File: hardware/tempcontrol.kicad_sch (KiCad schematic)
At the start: 17 parts, among them J10 FAN2, J9 FAN1, U12 EMC2305-x-AP

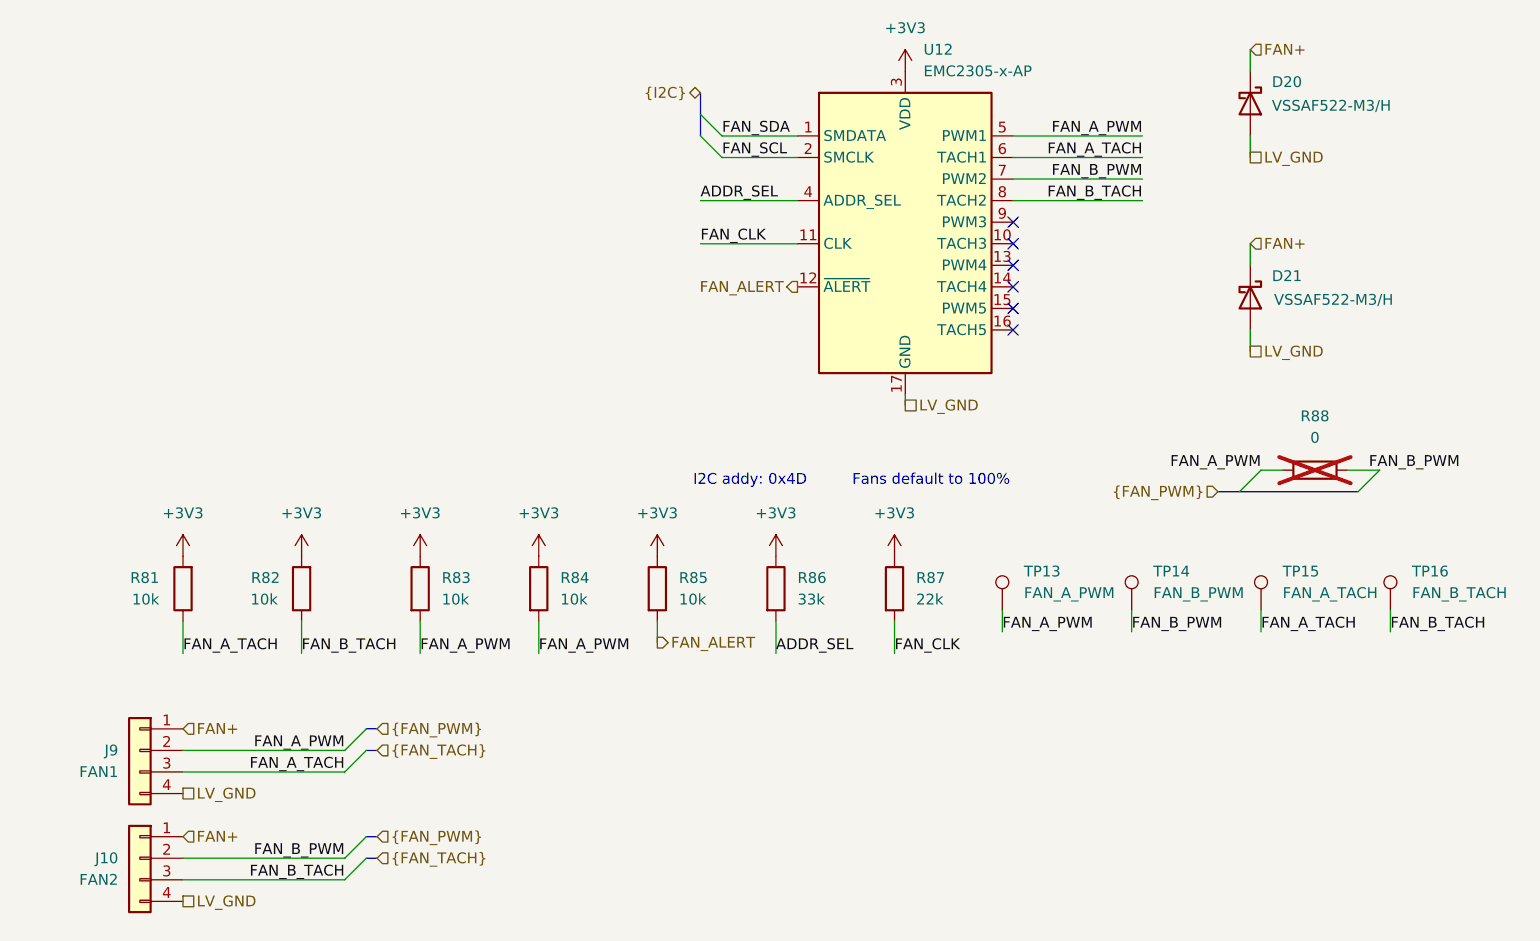
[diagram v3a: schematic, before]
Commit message: fixed up labels
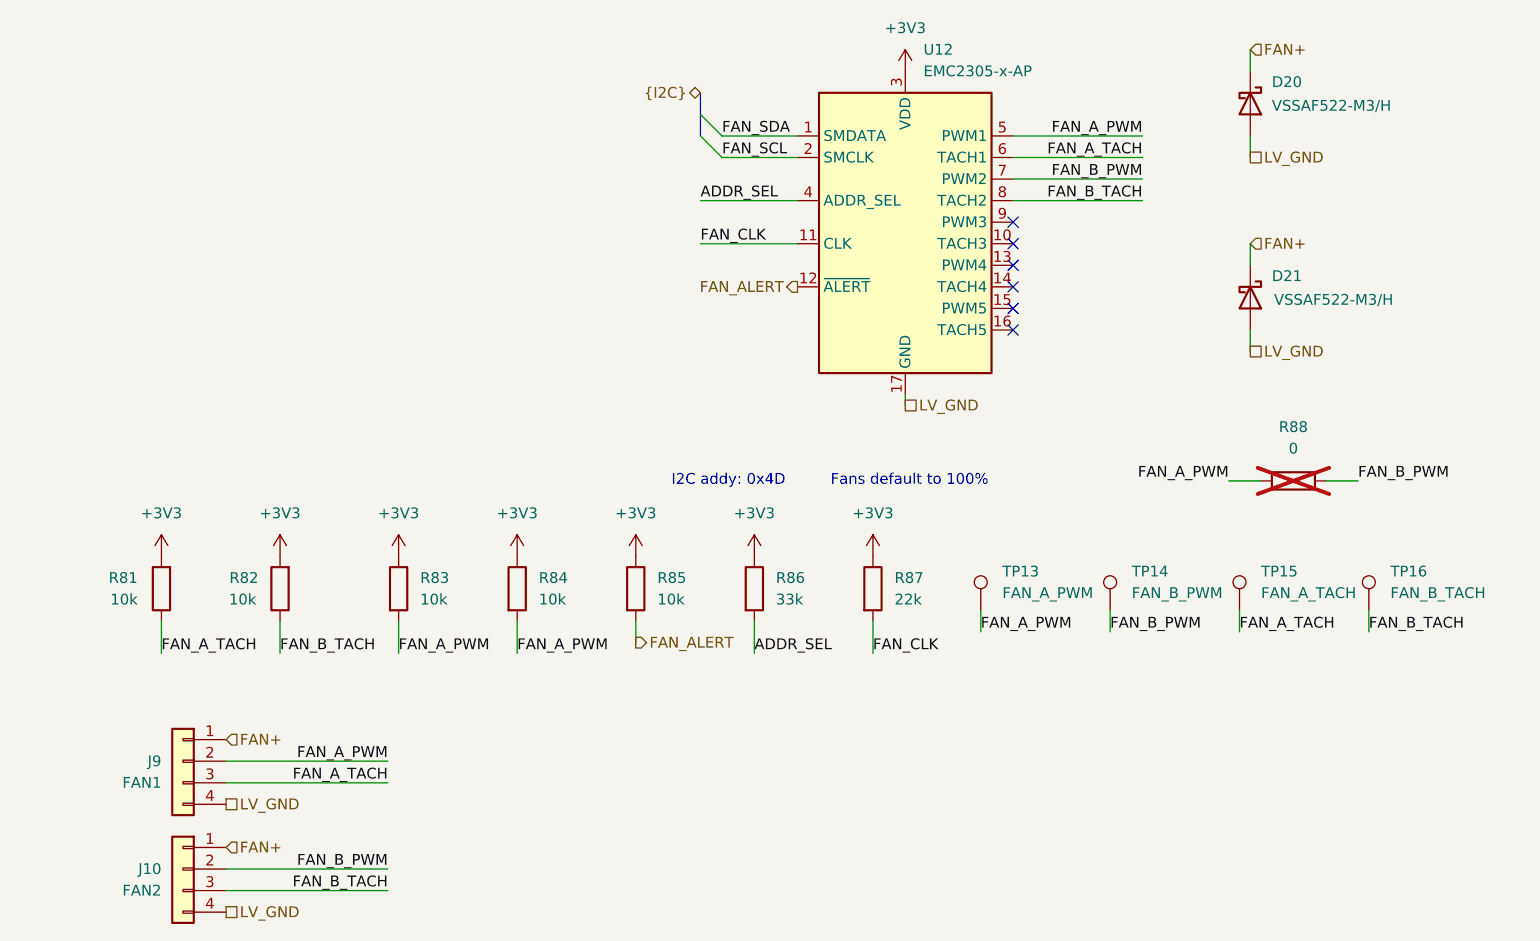
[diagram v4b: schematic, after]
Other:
- moved on the sheet: J10, J9, R81, R82, R83, R84, R85, R86, R87, R88, TP13, TP14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

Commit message: switch branch
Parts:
- renumbered R81 to R86, R82 to R87, R83 to R88, R84 to R89, R85 to R90, R86 to R91, R87 to R92, R88 to R93, TP13 to TP17, TP14 to TP18, TP15 to TP19, TP16 to TP20
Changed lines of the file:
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@@
 		(dnp no)
 		(fields_autoplaced yes)
-		(property "Reference" "R85"
+		(property "Reference" "R90"
 			(at 95.25 88.8999 0)
 			(show_name no)
@@
 			(project "PS-LVCarrier"
 				(path "/9bab2d9d-20f3-40ef-8545-e1299efec47e/f9fba8b7-0cf3-4419-9ae4-4e9c55277e07"
-					(reference "R85")
+					(reference "R90")
 					(unit 1)
 				)
@@
 		(dnp no)
 		(fields_autoplaced yes)
-		(property "Reference" "R84"
+		(property "Reference" "R89"
 			(at 81.28 88.8999 0)
 			(show_name no)
@@
 			(project "PS-LVCarrier"
 				(path "/9bab2d9d-20f3-40ef-8545-e1299efec47e/f9fba8b7-0cf3-4419-9ae4-4e9c55277e07"
-					(reference "R84")
+					(reference "R89")
 					(unit 1)
 				)
@@
 		(dnp no)
 		(fields_autoplaced yes)
-		(property "Reference" "TP16"
+		(property "Reference" "TP20"
 			(at 181.61 88.1379 0)
 			(show_name no)
@@
 			(project "PS-LVCarrier"
 				(path "/9bab2d9d-20f3-40ef-8545-e1299efec47e/f9fba8b7-0cf3-4419-9ae4-4e9c55277e07"
-					(reference "TP16")
+					(reference "TP20")
 					(unit 1)
 				)
@@
 		(dnp no)
 		(fields_autoplaced yes)
-		(property "Reference" "#PWR0104"
+		(property "Reference" "#PWR086"
 			(at 124.46 33.02 0)
 			(hide yes)
@@
 			(project "PS-LVCarrier"
 				(path "/9bab2d9d-20f3-40ef-8545-e1299efec47e/f9fba8b7-0cf3-4419-9ae4-4e9c55277e07"
-					(reference "#PWR0104")
+					(reference "#PWR086")
 					(unit 1)
 				)
@@
 		(dnp no)
 		(fields_autoplaced yes)
-		(property "Reference" "R83"
+		(property "Reference" "R88"
 			(at 67.31 88.8999 0)
 			(show_name no)
@@
 			(project "PS-LVCarrier"
 				(path "/9bab2d9d-20f3-40ef-8545-e1299efec47e/f9fba8b7-0cf3-4419-9ae4-4e9c55277e07"
-					(reference "R83")
+					(reference "R88")
 					(unit 1)
 				)
@@
 		(dnp no)
 		(fields_autoplaced yes)
-		(property "Reference" "#PWR097"
+		(property "Reference" "#PWR079"
 			(at 36.83 90.17 0)
 			(hide yes)
@@
 			(project "PS-LVCarrier"
 				(path "/9bab2d9d-20f3-40ef-8545-e1299efec47e/f9fba8b7-0cf3-4419-9ae4-4e9c55277e07"
-					(reference "#PWR097")
+					(reference "#PWR079")
 					(unit 1)
 				)
@@
 		(dnp no)
 		(fields_autoplaced yes)
-		(property "Reference" "TP15"
+		(property "Reference" "TP19"
 			(at 166.37 88.1379 0)
 			(show_name no)
@@
 			(project "PS-LVCarrier"
 				(path "/9bab2d9d-20f3-40ef-8545-e1299efec47e/f9fba8b7-0cf3-4419-9ae4-4e9c55277e07"
-					(reference "TP15")
+					(reference "TP19")
 					(unit 1)
 				)
@@
 		(in_pos_files yes)
 		(dnp no)
-		(property "Reference" "R82"
+		(property "Reference" "R87"
 			(at 48.26 88.9 0)
 			(show_name no)
@@
 			(project "PS-LVCarrier"
 				(path "/9bab2d9d-20f3-40ef-8545-e1299efec47e/f9fba8b7-0cf3-4419-9ae4-4e9c55277e07"
-					(reference "R82")
+					(reference "R87")
 					(unit 1)
 				)
@@
 		(dnp no)
 		(fields_autoplaced yes)
-		(property "Reference" "#PWR0100"
+		(property "Reference" "#PWR082"
 			(at 78.74 90.17 0)
 			(hide yes)
@@
 			(project "PS-LVCarrier"
 				(path "/9bab2d9d-20f3-40ef-8545-e1299efec47e/f9fba8b7-0cf3-4419-9ae4-4e9c55277e07"
-					(reference "#PWR0100")
+					(reference "#PWR082")
 					(unit 1)
 				)
@@
 		(dnp no)
 		(fields_autoplaced yes)
-		(property "Reference" "#PWR0101"
+		(property "Reference" "#PWR083"
 			(at 92.71 90.17 0)
 			(hide yes)
@@
 			(project "PS-LVCarrier"
 				(path "/9bab2d9d-20f3-40ef-8545-e1299efec47e/f9fba8b7-0cf3-4419-9ae4-4e9c55277e07"
-					(reference "#PWR0101")
+					(reference "#PWR083")
 					(unit 1)
 				)
@@
 		(dnp no)
 		(fields_autoplaced yes)
-		(property "Reference" "#PWR099"
+		(property "Reference" "#PWR081"
 			(at 64.77 90.17 0)
 			(hide yes)
@@
 			(project "PS-LVCarrier"
 				(path "/9bab2d9d-20f3-40ef-8545-e1299efec47e/f9fba8b7-0cf3-4419-9ae4-4e9c55277e07"
-					(reference "#PWR099")
+					(reference "#PWR081")
 					(unit 1)
 				)
@@
 		(dnp no)
 		(fields_autoplaced yes)
-		(property "Reference" "R86"
+		(property "Reference" "R91"
 			(at 109.22 88.8999 0)
 			(show_name no)
@@
 			(project "PS-LVCarrier"
 				(path "/9bab2d9d-20f3-40ef-8545-e1299efec47e/f9fba8b7-0cf3-4419-9ae4-4e9c55277e07"
-					(reference "R86")
+					(reference "R91")
 					(unit 1)
 				)
@@
 		(dnp no)
 		(fields_autoplaced yes)
-		(property "Reference" "TP14"
+		(property "Reference" "TP18"
 			(at 151.13 88.1379 0)
 			(show_name no)
@@
 			(project "PS-LVCarrier"
 				(path "/9bab2d9d-20f3-40ef-8545-e1299efec47e/f9fba8b7-0cf3-4419-9ae4-4e9c55277e07"
-					(reference "TP14")
+					(reference "TP18")
 					(unit 1)
 				)
@@
 		(dnp no)
 		(fields_autoplaced yes)
-		(property "Reference" "TP13"
+		(property "Reference" "TP17"
 			(at 135.89 88.1379 0)
 			(show_name no)
@@
 			(project "PS-LVCarrier"
 				(path "/9bab2d9d-20f3-40ef-8545-e1299efec47e/f9fba8b7-0cf3-4419-9ae4-4e9c55277e07"
-					(reference "TP13")
+					(reference "TP17")
 					(unit 1)
 				)
@@
 		(dnp no)
 		(fields_autoplaced yes)
-		(property "Reference" "#PWR0103"
+		(property "Reference" "#PWR085"
 			(at 120.65 90.17 0)
 			(hide yes)
@@
 			(project "PS-LVCarrier"
 				(path "/9bab2d9d-20f3-40ef-8545-e1299efec47e/f9fba8b7-0cf3-4419-9ae4-4e9c55277e07"
-					(reference "#PWR0103")
+					(reference "#PWR085")
 					(unit 1)
 				)
@@
 		(dnp no)
 		(fields_autoplaced yes)
-		(property "Reference" "R87"
+		(property "Reference" "R92"
 			(at 123.19 88.8999 0)
 			(show_name no)
@@
 			(project "PS-LVCarrier"
 				(path "/9bab2d9d-20f3-40ef-8545-e1299efec47e/f9fba8b7-0cf3-4419-9ae4-4e9c55277e07"
-					(reference "R87")
+					(reference "R92")
 					(unit 1)
 				)
@@
 		(dnp yes)
 		(fields_autoplaced yes)
-		(property "Reference" "R88"
+		(property "Reference" "R93"
 			(at 170.18 71.12 90)
 			(show_name no)
@@
 			(project "PS-LVCarrier"
 				(path "/9bab2d9d-20f3-40ef-8545-e1299efec47e/f9fba8b7-0cf3-4419-9ae4-4e9c55277e07"
-					(reference "R88")
+					(reference "R93")
 					(unit 1)
 				)
@@
 		(in_pos_files yes)
 		(dnp no)
-		(property "Reference" "R81"
+		(property "Reference" "R86"
 			(at 34.036 88.9 0)
 			(show_name no)
@@
 			(project "PS-LVCarrier"
 				(path "/9bab2d9d-20f3-40ef-8545-e1299efec47e/f9fba8b7-0cf3-4419-9ae4-4e9c55277e07"
-					(reference "R81")
+					(reference "R86")
 					(unit 1)
 				)
@@
 		(dnp no)
 		(fields_autoplaced yes)
-		(property "Reference" "#PWR098"
+		(property "Reference" "#PWR080"
 			(at 50.8 90.17 0)
 			(hide yes)
@@
 			(project "PS-LVCarrier"
 				(path "/9bab2d9d-20f3-40ef-8545-e1299efec47e/f9fba8b7-0cf3-4419-9ae4-4e9c55277e07"
-					(reference "#PWR098")
+					(reference "#PWR080")
 					(unit 1)
 				)
@@
 		(dnp no)
 		(fields_autoplaced yes)
-		(property "Reference" "#PWR0102"
+		(property "Reference" "#PWR084"
 			(at 106.68 90.17 0)
 			(hide yes)
@@
 			(project "PS-LVCarrier"
 				(path "/9bab2d9d-20f3-40ef-8545-e1299efec47e/f9fba8b7-0cf3-4419-9ae4-4e9c55277e07"
-					(reference "#PWR0102")
-					(unit 1)
-				)
+					(reference "#PWR084")
+					(unit 1)
+				)

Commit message: most reviews addressed oops
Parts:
- removed D21: VSSAF522-M3/H, UTSVT_Passive:SODFL5026X125N, symbol Diode:C3D25170H
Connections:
- net +3V3: no longer U12.3 (VDD)
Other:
- moved on the sheet: D20, J10, J9, U12

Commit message: progress!
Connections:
- net +3V3: now also U12.3 (VDD)
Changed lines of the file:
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@@
 	(symbol
 		(lib_id "power:+3V3")
-		(at 124.46 29.21 0)
+		(at 130.81 29.21 0)
 		(unit 1)
 		(body_style 1)
@@
 		(fields_autoplaced yes)
 		(property "Reference" "#PWR086"
-			(at 124.46 33.02 0)
+			(at 130.81 33.02 0)
 			(hide yes)
 			(show_name no)
@@
 		)
 		(property "Value" "+3V3"
-			(at 124.46 24.13 0)
+			(at 130.81 24.13 0)
 			(show_name no)
 			(do_not_autoplace no)
@@
 		)
 		(property "Footprint" ""
-			(at 124.46 29.21 0)
+			(at 130.81 29.21 0)
 			(hide yes)
 			(show_name no)
@@
 		)
 		(property "Datasheet" ""
-			(at 124.46 29.21 0)
+			(at 130.81 29.21 0)
 			(hide yes)
 			(show_name no)
@@
 		)
 		(property "Description" "Power symbol creates a global label with name \"+3V3\""
-			(at 124.46 29.21 0)
+			(at 130.81 29.21 0)
 			(hide yes)
 			(show_name no)

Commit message: review ts
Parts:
- renumbered D20 to D7, J10 to J7, J9 to J8, R86 to R19, R87 to R20, R88 to R21, R89 to R22, R90 to R23, R91 to R24, R92 to R25, R93 to R26, TP17 to TP5, TP18 to TP6, TP19 to TP7, TP20 to TP8, U12 to U2
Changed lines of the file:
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@@
 		(dnp no)
 		(fields_autoplaced yes)
-		(property "Reference" "U12"
+		(property "Reference" "U2"
 			(at 134.112 26.416 0)
 			(show_name no)
@@
 			(project "PS-LVCarrier"
 				(path "/9bab2d9d-20f3-40ef-8545-e1299efec47e/f9fba8b7-0cf3-4419-9ae4-4e9c55277e07"
-					(reference "U12")
+					(reference "U2")
 					(unit 1)
 				)
@@
 		(dnp no)
 		(fields_autoplaced yes)
-		(property "Reference" "R90"
+		(property "Reference" "R23"
 			(at 95.25 88.8999 0)
 			(show_name no)
@@
 			(project "PS-LVCarrier"
 				(path "/9bab2d9d-20f3-40ef-8545-e1299efec47e/f9fba8b7-0cf3-4419-9ae4-4e9c55277e07"
-					(reference "R90")
+					(reference "R23")
 					(unit 1)
 				)
@@
 		(dnp no)
 		(fields_autoplaced yes)
-		(property "Reference" "R89"
+		(property "Reference" "R22"
 			(at 81.28 88.8999 0)
 			(show_name no)
@@
 			(project "PS-LVCarrier"
 				(path "/9bab2d9d-20f3-40ef-8545-e1299efec47e/f9fba8b7-0cf3-4419-9ae4-4e9c55277e07"
-					(reference "R89")
+					(reference "R22")
 					(unit 1)
 				)
@@
 		(dnp no)
 		(fields_autoplaced yes)
-		(property "Reference" "TP20"
+		(property "Reference" "TP8"
 			(at 181.61 88.1379 0)
 			(show_name no)
@@
 			(project "PS-LVCarrier"
 				(path "/9bab2d9d-20f3-40ef-8545-e1299efec47e/f9fba8b7-0cf3-4419-9ae4-4e9c55277e07"
-					(reference "TP20")
+					(reference "TP8")
 					(unit 1)
 				)
@@
 		(dnp no)
 		(fields_autoplaced yes)
-		(property "Reference" "#PWR086"
+		(property "Reference" "#PWR031"
 			(at 130.81 33.02 0)
 			(hide yes)
@@
 			(project "PS-LVCarrier"
 				(path "/9bab2d9d-20f3-40ef-8545-e1299efec47e/f9fba8b7-0cf3-4419-9ae4-4e9c55277e07"
-					(reference "#PWR086")
+					(reference "#PWR031")
 					(unit 1)
 				)
@@
 		(dnp no)
 		(fields_autoplaced yes)
-		(property "Reference" "R88"
+		(property "Reference" "R21"
 			(at 67.31 88.8999 0)
 			(show_name no)
@@
 			(project "PS-LVCarrier"
 				(path "/9bab2d9d-20f3-40ef-8545-e1299efec47e/f9fba8b7-0cf3-4419-9ae4-4e9c55277e07"
-					(reference "R88")
+					(reference "R21")
 					(unit 1)
 				)
@@
 		(dnp no)
 		(fields_autoplaced yes)
-		(property "Reference" "#PWR079"
+		(property "Reference" "#PWR024"
 			(at 36.83 90.17 0)
 			(hide yes)
@@
 			(project "PS-LVCarrier"
 				(path "/9bab2d9d-20f3-40ef-8545-e1299efec47e/f9fba8b7-0cf3-4419-9ae4-4e9c55277e07"
-					(reference "#PWR079")
+					(reference "#PWR024")
 					(unit 1)
 				)
@@
 		(dnp no)
 		(fields_autoplaced yes)
-		(property "Reference" "TP19"
+		(property "Reference" "TP7"
 			(at 166.37 88.1379 0)
 			(show_name no)
@@
 			(project "PS-LVCarrier"
 				(path "/9bab2d9d-20f3-40ef-8545-e1299efec47e/f9fba8b7-0cf3-4419-9ae4-4e9c55277e07"
-					(reference "TP19")
+					(reference "TP7")
 					(unit 1)
 				)
@@
 		(in_pos_files yes)
 		(dnp no)
-		(property "Reference" "R87"
+		(property "Reference" "R20"
 			(at 48.26 88.9 0)
 			(show_name no)
@@
 			(project "PS-LVCarrier"
 				(path "/9bab2d9d-20f3-40ef-8545-e1299efec47e/f9fba8b7-0cf3-4419-9ae4-4e9c55277e07"
-					(reference "R87")
+					(reference "R20")
 					(unit 1)
 				)
@@
 		(dnp no)
 		(fields_autoplaced yes)
-		(property "Reference" "#PWR082"
+		(property "Reference" "#PWR027"
 			(at 78.74 90.17 0)
 			(hide yes)
@@
 			(project "PS-LVCarrier"
 				(path "/9bab2d9d-20f3-40ef-8545-e1299efec47e/f9fba8b7-0cf3-4419-9ae4-4e9c55277e07"
-					(reference "#PWR082")
+					(reference "#PWR027")
 					(unit 1)
 				)
@@
 		(dnp no)
 		(fields_autoplaced yes)
-		(property "Reference" "#PWR083"
+		(property "Reference" "#PWR028"
 			(at 92.71 90.17 0)
 			(hide yes)
@@
 			(project "PS-LVCarrier"
 				(path "/9bab2d9d-20f3-40ef-8545-e1299efec47e/f9fba8b7-0cf3-4419-9ae4-4e9c55277e07"
-					(reference "#PWR083")
+					(reference "#PWR028")
 					(unit 1)
 				)
@@
 		(dnp no)
 		(fields_autoplaced yes)
-		(property "Reference" "#PWR081"
+		(property "Reference" "#PWR026"
 			(at 64.77 90.17 0)
 			(hide yes)
@@
 			(project "PS-LVCarrier"
 				(path "/9bab2d9d-20f3-40ef-8545-e1299efec47e/f9fba8b7-0cf3-4419-9ae4-4e9c55277e07"
-					(reference "#PWR081")
+					(reference "#PWR026")
 					(unit 1)
 				)
@@
 		(dnp no)
 		(fields_autoplaced yes)
-		(property "Reference" "R91"
+		(property "Reference" "R24"
 			(at 109.22 88.8999 0)
 			(show_name no)
@@
 			(project "PS-LVCarrier"
 				(path "/9bab2d9d-20f3-40ef-8545-e1299efec47e/f9fba8b7-0cf3-4419-9ae4-4e9c55277e07"
-					(reference "R91")
+					(reference "R24")
 					(unit 1)
 				)
@@
 		(in_pos_files yes)
 		(dnp no)
-		(property "Reference" "J9"
+		(property "Reference" "J8"
 			(at 59.69 114.2999 0)
 			(show_name no)
@@
 			(project "PS-LVCarrier"
 				(path "/9bab2d9d-20f3-40ef-8545-e1299efec47e/f9fba8b7-0cf3-4419-9ae4-4e9c55277e07"
-					(reference "J9")
+					(reference "J8")
 					(unit 1)
 				)
@@
 		(in_pos_files yes)
 		(dnp no)
-		(property "Reference" "J10"
+		(property "Reference" "J7"
 			(at 25.4 114.2999 0)
 			(show_name no)
@@
 			(project "PS-LVCarrier"
 				(path "/9bab2d9d-20f3-40ef-8545-e1299efec47e/f9fba8b7-0cf3-4419-9ae4-4e9c55277e07"
-					(reference "J10")
+					(reference "J7")
 					(unit 1)
 				)
@@
 		(dnp no)
 		(fields_autoplaced yes)
-		(property "Reference" "TP18"
+		(property "Reference" "TP6"
 			(at 151.13 88.1379 0)
 			(show_name no)
@@
 			(project "PS-LVCarrier"
 				(path "/9bab2d9d-20f3-40ef-8545-e1299efec47e/f9fba8b7-0cf3-4419-9ae4-4e9c55277e07"
-					(reference "TP18")
+					(reference "TP6")
 					(unit 1)
 				)
@@
 		(dnp no)
 		(fields_autoplaced yes)
-		(property "Reference" "TP17"
+		(property "Reference" "TP5"
 			(at 135.89 88.1379 0)
 			(show_name no)
@@
 			(project "PS-LVCarrier"
 				(path "/9bab2d9d-20f3-40ef-8545-e1299efec47e/f9fba8b7-0cf3-4419-9ae4-4e9c55277e07"
-					(reference "TP17")
+					(reference "TP5")
 					(unit 1)
 				)
@@
 		(dnp no)
 		(fields_autoplaced yes)
-		(property "Reference" "#PWR085"
+		(property "Reference" "#PWR030"
 			(at 120.65 90.17 0)
 			(hide yes)
@@
 			(project "PS-LVCarrier"
 				(path "/9bab2d9d-20f3-40ef-8545-e1299efec47e/f9fba8b7-0cf3-4419-9ae4-4e9c55277e07"
-					(reference "#PWR085")
+					(reference "#PWR030")
 					(unit 1)
 				)
@@
 		(dnp no)
 		(fields_autoplaced yes)
-		(property "Reference" "R92"
+		(property "Reference" "R25"
 			(at 123.19 88.8999 0)
 			(show_name no)
@@
 			(project "PS-LVCarrier"
 				(path "/9bab2d9d-20f3-40ef-8545-e1299efec47e/f9fba8b7-0cf3-4419-9ae4-4e9c55277e07"
-					(reference "R92")
+					(reference "R25")
 					(unit 1)
 				)
@@
 		(in_pos_files yes)
 		(dnp no)
-		(property "Reference" "D20"
+		(property "Reference" "D7"
 			(at 177.8 40.64 90)
 			(show_name no)
@@
 			(project "PS-LVCarrier"
 				(path "/9bab2d9d-20f3-40ef-8545-e1299efec47e/f9fba8b7-0cf3-4419-9ae4-4e9c55277e07"
-					(reference "D20")
+					(reference "D7")
 					(unit 1)
 				)
@@
 		(dnp yes)
 		(fields_autoplaced yes)
-		(property "Reference" "R93"
+		(property "Reference" "R26"
 			(at 170.18 71.12 90)
 			(show_name no)
@@
 			(project "PS-LVCarrier"
 				(path "/9bab2d9d-20f3-40ef-8545-e1299efec47e/f9fba8b7-0cf3-4419-9ae4-4e9c55277e07"
-					(reference "R93")
+					(reference "R26")
 					(unit 1)
 				)
@@
 		(in_pos_files yes)
 		(dnp no)
-		(property "Reference" "R86"
+		(property "Reference" "R19"
 			(at 34.036 88.9 0)
 			(show_name no)
@@
 			(project "PS-LVCarrier"
 				(path "/9bab2d9d-20f3-40ef-8545-e1299efec47e/f9fba8b7-0cf3-4419-9ae4-4e9c55277e07"
-					(reference "R86")
+					(reference "R19")
 					(unit 1)
 				)
@@
 		(dnp no)
 		(fields_autoplaced yes)
-		(property "Reference" "#PWR080"
+		(property "Reference" "#PWR025"
 			(at 50.8 90.17 0)
 			(hide yes)
@@
 			(project "PS-LVCarrier"
 				(path "/9bab2d9d-20f3-40ef-8545-e1299efec47e/f9fba8b7-0cf3-4419-9ae4-4e9c55277e07"
-					(reference "#PWR080")
+					(reference "#PWR025")
 					(unit 1)
 				)
@@
 		(dnp no)
 		(fields_autoplaced yes)
-		(property "Reference" "#PWR084"
+		(property "Reference" "#PWR029"
 			(at 106.68 90.17 0)
 			(hide yes)
@@
 			(project "PS-LVCarrier"
 				(path "/9bab2d9d-20f3-40ef-8545-e1299efec47e/f9fba8b7-0cf3-4419-9ae4-4e9c55277e07"
-					(reference "#PWR084")
-					(unit 1)
-				)
+					(reference "#PWR029")
+					(unit 1)
+				)
